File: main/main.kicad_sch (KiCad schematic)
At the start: 158 parts, among them J1 Conn_02x07_Odd_Even, J10 Conn_01x05_Pin, J2 Conn_01x02_Pin, J3 Conn_01x02_Socket, J4 Conn_01x05_Pin, J5 Conn_01x05_Pin, J6 Conn_01x05_Pin, J7 Conn_01x05_Pin, J8 Conn_01x04_Pin, J9 Conn_01x04_Pin, P1 USB_C_Plug_USB2.0, Q1 2SK2623-TL, Q10 L-31ROPT1C, Q11 L-31ROPT1C, Q12 L-31ROPT1C, Q13 L-31ROPT1C, Q14 L-31ROPT1C, Q15 L-31ROPT1C, Q16 L-31ROPT1C, Q17 L-31ROPT1C, Q18 L-31ROPT1C, Q19 L-31ROPT1C, Q2 TJ60S04M3L, Q20 2SA1015, Q21 2SA1015, Q22 2SA1015, Q23 BSS138, Q24 BSS138, Q25 2SA1015, Q3 TJ60S04M3L, Q4 L-31ROPT1C, Q5 L-31ROPT1C, Q6 L-31ROPT1C, Q7 L-31ROPT1C, Q8 L-31ROPT1C, Q9 L-31ROPT1C, SW1 SW_SPST, SW2 SW_Push, SW3 SW_Push, SW4 SW_Push, U1 OKL-T/6-W12N-C, U10 MAX3485, U2 AZ1117-3.3, U3 STM32F405RGT6, U4 BNO055, U5 MAX3485, U6 MAX3485, U7 MAX3485, U8 ESP32-WROOM-32, U9 Interface_USB_CH340K, Y1 16MHz

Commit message: メイン基板回路図完成
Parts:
- added C27, C28, C29: 0.1uF, Capacitor_SMD:C_0603_1608Metric_Pad1.08x0.95mm_HandSolder, symbol Device:C
- added D19, D20, D21: LED, LED_SMD:LED_0603_1608Metric_Pad1.05x0.95mm_HandSolder, symbol Device:LED
- added R62, R63, R64, R65, R66, R67, R68, R69, R72, R73, R74, R75, R76, R77: 10k, Resistor_SMD:R_0603_1608Metric_Pad0.98x0.95mm_HandSolder, symbol Device:R
- added R70, R71, R78: 1k, Resistor_SMD:R_0603_1608Metric_Pad0.98x0.95mm_HandSolder, symbol Device:R
- added SW10, SW5: SW_DIP_x04, Button_Switch_SMD:SW_DIP_SPSTx04_Slide_Copal_CHS-04B_W7.62mm_P1.27mm, symbol Switch:SW_DIP_x04
- added SW11, SW6, SW7: SW_SPDT, Tomoshibi_Library:SW_Slide_3P_SPDT, symbol Switch:SW_SPDT
- added SW12, SW8, SW9: SW_Push, Button_Switch_SMD:SW_Push_1P1T_NO_6x6mm_H9.5mm, symbol Switch:SW_Push
- added TP1, TP2, TP3, TP4: TestPoint, TestPoint:TestPoint_THTPad_D2.0mm_Drill1.0mm, symbol Connector:TestPoint
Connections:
- net F405RX is gone; now on net ESP_RX: U8.27 (IO16)
- net F405TX is gone; now on net ESP_TX: U8.28 (IO17)
- net +12V: now also TP1.1
- net +3.3V: now also R68.1, R69.1, R77.1, SW10.1, SW10.2, SW10.3, SW10.4, SW11.2 (B), SW5.1, SW5.2, SW5.3, SW5.4, SW6.2 (B), SW7.2 (B), TP3.1
- net +5V: now also TP2.1
- net GND: now also C27.1, C28.1, C29.1, R62.2, R63.2, R64.2, R65.2, R66.2, R67.2, R70.2, R71.2, R72.2, R73.2, R74.2, R75.2, R76.2, R78.2, SW12.2, SW8.2, SW9.2, TP4.1
- net MD_A: no longer J4.5 (Pin_5), J5.5 (Pin_5), R41.1, U5.7 (B)
- net DIPSW1: now reaches U3.2 (PC13)
- net DIPSW1: now also R63.1, SW5.7
- net DIPSW2: now reaches U3.3 (PC14)
- net DIPSW2: now also R64.1, SW5.6
- net DIPSW3: now reaches U3.4 (PC15)
- net DIPSW3: now also R65.1, SW5.5
- net LED1: now reaches U3.44 (PA11)
- net LED1: now also D20.2 (A)
- net LED0: now reaches U3.45 (PA12)
- net LED0: now also D19.2 (A)
- net TactSW1: now reaches U3.50 (PA15)
- net TactSW1: now also C28.2, R69.2, SW9.1
- net TactSW0: now reaches U3.56 (PB4)
- net TactSW0: now also C27.2, R68.2, SW8.1
- net SlideSW1: now reaches U3.57 (PB5)
- net SlideSW1: now also R67.1, SW7.1 (A)
- net SlideSW0: now reaches U3.61 (PB8)
- net SlideSW0: now also R66.1, SW6.1 (A)
- net DIPSW0: now reaches U3.62 (PB9)
- net DIPSW0: now also R62.1, SW5.8
- net ESP_SlideSW: now reaches U8.10 (IO25)
- net ESP_SlideSW: now also R76.1, SW11.1 (A)
- net ESP_TactSW: now reaches U8.11 (IO26)
- net ESP_TactSW: now also C29.2, R77.2, SW12.1
- net ESP_LED: now reaches U8.12 (IO27)
- net ESP_LED: now also D21.2 (A)
- net ESP_DIPSW0: now reaches U8.6 (IO34)
- net ESP_DIPSW0: now also R72.1, SW10.8
- net ESP_DIPSW1: now reaches U8.7 (IO35)
- net ESP_DIPSW1: now also R73.1, SW10.7
- net ESP_DIPSW2: now reaches U8.8 (IO32)
- net ESP_DIPSW2: now also R74.1, SW10.6
- net ESP_DIPSW3: now reaches U8.9 (IO33)
- net ESP_DIPSW3: now also R75.1, SW10.5
- new net: D20.1 (K), R71.1
- new net: D19.1 (K), R70.1
- new net: D21.1 (K), R78.1
- new net MD_B: J4.5 (Pin_5), J5.5 (Pin_5), R41.1, U5.7 (B)
- no-connect marks 15 -> 44
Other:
- note added: "BOOT"
- note added: "RESET"
- note added: "UI"
- note added: "サブマイコン"
- note added: "テストポイント"
- note added: "書き込み"
- moved on the sheet: C21, C22, C23, C24, P1, Q23, Q24, R53, R54, R55, R56, SW2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

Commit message: MD基板開発データ追加
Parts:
- added D22, D23, D24: LED, LED_SMD:LED_0603_1608Metric_Pad1.05x0.95mm_HandSolder, symbol Device:LED
- added R79: 6.8k, Resistor_SMD:R_0603_1608Metric_Pad0.98x0.95mm_HandSolder, symbol Device:R
- added R80: 2.2k, Resistor_SMD:R_0603_1608Metric_Pad0.98x0.95mm_HandSolder, symbol Device:R
- added R81: 1k, Resistor_SMD:R_0603_1608Metric_Pad0.98x0.95mm_HandSolder, symbol Device:R
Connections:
- net +12V: now also D22.2 (A)
- net +3.3V: now also D24.2 (A)
- net +5V: now also D23.2 (A)
- net GND: now also R79.2, R80.2, R81.2
- new net: D23.1 (K), R80.1
- new net: D24.1 (K), R81.1
- new net: D22.1 (K), R79.1
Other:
- note added: "電源LED"
- moved on the sheet: TP1, TP2, TP3, TP4

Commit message: 指摘された間違いを修正
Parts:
- removed Q1: 2SK2623-TL, Package_TO_SOT_SMD:TO-252-3_TabPin2, symbol Device:Q_NMOS_GDS
- removed R61: 10k, Resistor_SMD:R_0603_1608Metric_Pad0.98x0.95mm_HandSolder, symbol Device:R
- added F1: 20A, Tomoshibi_Library:Fuseholder_Keystone_3557, symbol Device:Fuse
- added Q1: BSS138, Package_TO_SOT_SMD:SOT-23, symbol Transistor_FET:BSS138
- R3: value 10k -> 100k
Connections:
- net +3.3V: now also Q20.1 (E), Q21.1 (E), Q22.1 (E), Q25.1 (E); no longer Q20.2 (C), Q21.2 (C), Q22.2 (C), Q25.2 (C)
- net BAT: now also F1.1; no longer Q2.2 (D), SW1.1 (A)
- net GND: now also Q1.2 (S)
- net MD_TX: no longer Q20.1 (E), R44.1, U5.2 (~{RE}), U5.3 (DE)
- net Uart1_TX: no longer Q21.1 (E), R46.1, U6.2 (~{RE}), U6.3 (DE)
- net Uart2_TX: no longer Q22.1 (E), R50.1, U7.2 (~{RE}), U7.3 (DE)
- net Uart3_TX: no longer Q25.1 (E), R58.1, U10.2 (~{RE}), U10.3 (DE)
- net at R1.1, SW1.2 (B): now also Q1.1 (G)
- net at R2.2: now also Q1.3 (D)
- new net: F1.2, Q2.2 (D), SW1.1 (A)
- new net: Q20.2 (C), R44.1, U5.2 (~{RE}), U5.3 (DE)
- new net: Q25.2 (C), R58.1, U10.2 (~{RE}), U10.3 (DE)
- new net: Q22.2 (C), R50.1, U7.2 (~{RE}), U7.3 (DE)
- new net: Q21.2 (C), R46.1, U6.2 (~{RE}), U6.3 (DE)
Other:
- moved on the sheet: C1, C2, JP1, MES1, Q2, Q3, R1, R2, R3, SW1

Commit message: 修正版回路図完成
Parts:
- removed D22: LED, LED_SMD:LED_0603_1608Metric_Pad1.05x0.95mm_HandSolder, symbol Device:LED
- removed J1: Conn_02x07_Odd_Even, Tomoshibi_Library:BoxHeader_2x07_P1.27mm_Horizontal, symbol Connector_Generic:Conn_02x07_Odd_Even
- removed J10, J7: Conn_01x05_Pin, Connector_JST:JST_XH_B5B-XH-A_1x05_P2.50mm_Vertical, symbol Connector:Conn_01x05_Pin
- removed J2: Conn_01x02_Pin, Connector_AMASS:AMASS_XT30U-M_1x02_P5.0mm_Vertical, symbol Connector:Conn_01x02_Pin
- removed J3: Conn_01x02_Socket, Connector_AMASS:AMASS_XT30U-F_1x02_P5.0mm_Vertical, symbol Connector:Conn_01x02_Socket
- removed J9: Conn_01x04_Pin, Connector_JST:JST_XH_B4B-XH-A_1x04_P2.50mm_Vertical, symbol Connector:Conn_01x04_Pin
- removed Q1, Q23, Q24: BSS138, Package_TO_SOT_SMD:SOT-23, symbol Transistor_FET:BSS138
- removed Q10, Q11, Q12, Q13, Q14, Q15, Q16, Q17, Q18, Q19, Q4, Q5, Q6, Q7, Q8, Q9: L-31ROPT1C, Tomoshibi_Library:L-31ROPT1C, symbol Device:Q_Photo_NPN
- removed Q2: TJ60S04M3L, Package_TO_SOT_THT:TO-251-3_Vertical, symbol Device:Q_PMOS_GDS
- removed Q20, Q21, Q22, Q25: 2SA1015, Package_TO_SOT_THT:TO-92_Inline, symbol Transistor_BJT:2SA1015
- removed SW4: SW_Push, Button_Switch_SMD:SW_Push_1P1T_NO_6x6mm_H9.5mm, symbol Switch:SW_Push
- removed SW5: SW_DIP_x04, Button_Switch_SMD:SW_DIP_SPSTx04_Slide_Copal_CHS-04B_W7.62mm_P1.27mm, symbol Switch:SW_DIP_x04
- removed SW7: SW_SPDT, Tomoshibi_Library:SW_Slide_3P_SPDT, symbol Switch:SW_SPDT
- removed TP2, TP3, TP4: TestPoint, TestPoint:TestPoint_THTPad_D2.0mm_Drill1.0mm, symbol Connector:TestPoint
- removed U10: MAX3485, Package_SO:SOP-8_3.76x4.96mm_P1.27mm, symbol Interface_UART:MAX3485
- removed U2: AZ1117-3.3, Package_TO_SOT_SMD:SOT-223-3_TabPin2, symbol Regulator_Linear:AZ1117-3.3
- removed U3: STM32F405RGT6, Package_QFP:LQFP-64_10x10mm_P0.5mm, symbol Tomoshibi_Library:STM32F405RGT6
- removed U4: BNO055, Tomoshibi_Library:Sensor_Motion_Aktk_BNO055, symbol Sensor_Motion:BNO055
- removed U8: ESP32-WROOM-32, RF_Module:ESP32-WROOM-32, symbol RF_Module:ESP32-WROOM-32
- removed U9: Interface_USB_CH340K, Package_SO:SSOP-10_3.9x4.9mm_P1.00mm, symbol Tomoshibi_Library:Interface_USB_CH340K
- added C30: 0.1uF, Capacitor_SMD:C_0603_1608Metric_Pad1.08x0.95mm_HandSolder, symbol Device:C
- added D22: MA10EB045, Tomoshibi_Library:Diode_DO-221BC, symbol Device:D_Schottky
- added D25: OSBL1608C1A, LED_SMD:LED_0603_1608Metric_Pad1.05x0.95mm_HandSolder, symbol Device:LED
- added J1: Conn_01x02_Pin, Connector_AMASS:AMASS_XT30U-M_1x02_P5.0mm_Vertical, symbol Connector:Conn_01x02_Pin
- added J2, J3: Conn_01x05_Pin, Connector_JST:JST_XH_B5B-XH-A_1x05_P2.50mm_Vertical, symbol Connector:Conn_01x05_Pin
- added J7: Conn_01x04_Pin, Connector_JST:JST_XH_B4B-XH-A_1x04_P2.50mm_Vertical, symbol Connector:Conn_01x04_Pin
- added J9: Conn_02x07_Odd_Even, Tomoshibi_Library:BoxHeader_2x07_P1.27mm_Horizontal, symbol Connector_Generic:Conn_02x07_Odd_Even
- added Q1: TJ60S04M3L, Tomoshibi_Library:DPAK+ 2-7M1A, symbol Device:Q_PMOS_GDS
- added Q10, Q11, Q12, Q13, Q14, Q15, Q16, Q17, Q18, Q19, Q20, Q21, Q22, Q23, Q8, Q9: NJL7502L, LED_THT:LED_D3.0mm, symbol Device:Q_Photo_NPN_EC
- added Q2: BSS138, Package_TO_SOT_SMD:SOT-23, symbol Transistor_FET:BSS138
- added Q24, Q25: 2SC3325, Package_TO_SOT_SMD:SOT-23-3, symbol Device:Q_NPN_BEC
- added Q4, Q5, Q6, Q7: 2SA1037AK, Package_TO_SOT_SMD:SOT-23-3, symbol Transistor_BJT:2SA1015
- added R61, R82: 10k, Resistor_SMD:R_0603_1608Metric_Pad0.98x0.95mm_HandSolder, symbol Device:R
- added R83: 1k, Resistor_SMD:R_0603_1608Metric_Pad0.98x0.95mm_HandSolder, symbol Device:R
- added SW4: SW_DIP_x04, Button_Switch_SMD:SW_DIP_SPSTx04_Slide_Copal_CHS-04B_W7.62mm_P1.27mm, symbol Switch:SW_DIP_x04
- added SW5: SW_SPDT, Tomoshibi_Library:SW_Slide_3P_SPDT, symbol Switch:SW_SPDT
- added SW7: SW_Push, Button_Switch_SMD:SW_Push_1P1T_NO_6x6mm_H9.5mm, symbol Switch:SW_Push
- added U10: Interface_USB_CH340K, Package_SO:SSOP-10_3.9x4.9mm_P1.00mm, symbol Tomoshibi_Library:Interface_USB_CH340K
- added U2: RT9080-33GJ5, Package_TO_SOT_SMD:TSOT-23-5, symbol Tomoshibi_Library:RT9080-33GJ5
- added U3: BNO055, Tomoshibi_Library:Sensor_Motion_Aktk_BNO055, symbol Tomoshibi_Library:BNO055
- added U4: STM32F405RGTx, Package_QFP:LQFP-64_10x10mm_P0.5mm, symbol Tomoshibi_Library:STM32F405RGTx
- added U8: MAX3485, Package_SO:SOP-8_3.76x4.96mm_P1.27mm, symbol Interface_UART:MAX3485
- added U9: ESP32-WROOM-32E, RF_Module:ESP32-WROOM-32D, symbol RF_Module:ESP32-WROOM-32E
- C13, C14: value 2.2uF -> 0.1uF
- C16, C17: value 0.1uF -> 2.2uF
- C19, C20: value 15pF -> 0.1uF
- C2: footprint Capacitor_SMD:CP_Elec_8x10 -> Capacitor_SMD:CP_Elec_8x10.5
- C23: value 0.1uF -> 22uF; footprint Capacitor_SMD:C_0603_1608Metric_Pad1.08x0.95mm_HandSolder -> Capacitor_SMD:C_0805_2012Metric_Pad1.18x1.45mm_HandSolder
- C24: value 22uF -> 0.1uF; footprint Capacitor_SMD:C_0805_2012Metric_Pad1.18x1.45mm_HandSolder -> Capacitor_SMD:C_0603_1608Metric_Pad1.08x0.95mm_HandSolder
- C5: value 10uF -> 1uF
- C6: value 22uF -> 1uF; footprint Capacitor_SMD:C_0805_2012Metric_Pad1.18x1.45mm_HandSolder -> Capacitor_SMD:C_0603_1608Metric_Pad1.08x0.95mm_HandSolder
- C7, C8: value 0.1uF -> 47pF
- D10, D11, D12, D13, D14, D15, D16, D17, D18, D6, D7, D8, D9: value OSI5120641E -> OSG8HA3Z74A; footprint LED_SMD:LED_1206_3216Metric_Pad1.42x1.75mm_HandSolder -> LED_THT:LED_D3.0mm
- D19, D20, D21: value LED -> OSG8HA3Z74A; footprint LED_SMD:LED_0603_1608Metric_Pad1.05x0.95mm_HandSolder -> LED_THT:LED_D3.0mm
- D23, D24: value LED -> OSBL1608C1A
- D3, D4, D5: value OSI5120641E -> OSR50603C1E; footprint LED_SMD:LED_1206_3216Metric_Pad1.42x1.75mm_HandSolder -> LED_SMD:LED_0603_1608Metric_Pad1.05x0.95mm_HandSolder
- Q3: footprint Package_TO_SOT_SMD:TO-252-2 -> Tomoshibi_Library:DPAK+ 2-7M1A
- R10: value 10k -> 200
- R11: value 1k -> 6.8k
- R12, R16, R20, R24, R28: value 10k -> 2.2k
- R14, R18, R22, R26: value 10k -> 7.5k
- R15, R19, R23, R27: value 1k -> 20k
- R17, R21, R25, R29: value 1k -> 2.2k
- R30, R32, R34, R36, R38, R40, R56, R72: value 10k -> 1k
- R31, R33, R35, R37, R70, R78, R8, R81, R9: value 1k -> 10k
- R4: value 1.3K -> 10k
- R41, R47, R51, R59, R80: value 2.2k -> 10k
- R42, R48, R52, R60: value 2.2k -> 1k
- R43, R45, R49, R57: value 7.5k -> 10k
- R44, R46, R50, R58: value 20k -> 1k
- R53: value 5.1k -> 10k
- R54: value 5.1k -> 1k
- R6: value 1.2k -> 1.3K
- R7: value 10k -> 1.2k
- R73, R74: value 10k -> 5.1k
- R79: value 6.8k -> 10k
- SW2: footprint Button_Switch_SMD:SW_Push_1P1T_NO_6x6mm_H9.5mm -> Tomoshibi_Library:SW_Push_6.1x6.1mm
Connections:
- net DIPSW0 is gone; now on net +3.3V: R62.1
- net LED0 is gone; now on net +3.3V: D19.2 (A)
- net LED1 is gone; now on net +3.3V: D20.2 (A)
- net MD_TX is gone; now on net MAIN_RX/MD_TX: U5.1 (RO)
- net Uart1_TX is gone; now on net MAIN1_RX/Device1_TX: U6.1 (RO)
- net Uart2_TX is gone; now on net MAIN2_RX/Device2_TX: U7.1 (RO)
- net Uart3_A is gone; now on net GND: R59.2
- net Uart3_B is gone; now on an unnamed net: R60.1
- net Uart3_RX is gone; now on net Line13: R57.1
- net +12V: now also D3.2 (A), D22.2 (A); no longer J4.2 (Pin_2), J5.2 (Pin_2), J6.2 (Pin_2), TP1.1
- net +3.3V: now also C13.1, C14.1, C15.1, C19.1, C20.1, C22.1, C23.1, C29.1, D21.2 (A), R16.1, R20.1, R24.1, R28.1, R70.1, R8.1, R9.1, J9.3 (Pin_3), Q10.2 (C), Q11.2 (C), Q12.2 (C), Q13.2 (C), Q14.2 (C), Q15.2 (C), Q16.2 (C), Q17.2 (C), Q18.2 (C), Q19.2 (C), Q20.2 (C), Q21.2 (C), Q22.2 (C), Q23.2 (C), Q4.1 (E), Q5.1 (E), Q6.1 (E), Q7.1 (E), Q8.2 (C), Q9.2 (C), R82.1, SW4.1, SW4.2, SW4.3, SW4.4, SW5.2 (B), U10.10 (V3), U10.7 (VCC), U3.1 (VIN), U4.1 (VBAT), U4.13 (VDDA), U4.19 (VDD), U4.32 (VDD), U4.48 (VDD), U4.64 (VDD), U8.8 (VCC), U9.2 (VDD); no longer C15.2, C16.1, C17.1, C24.1, C25.1, C6.1, C7.1, C8.1, C9.1, D2.2 (A), D24.2 (A), D3.2 (A), D4.2 (A), R39.1, R40.1, R42.1, R47.1, R51.1, R55.1, R56.1, R59.1, R68.1, R77.1
- net +5V: now also D4.2 (A), R7.1, J2.3 (Pin_3), J3.3 (Pin_3), J7.2 (Pin_2), U2.1 (VIN), U2.3 (EN); no longer D23.2 (A), R6.1
- net BAT: now also J1.2 (Pin_2)
- net BOOT: now also C28.2, SW9.1, Q25.3 (C), U9.25 (IO0); no longer C23.2, R56.2, SW3.1
- net ESP_DIPSW0: now also R77.1, U9.6 (IO34); no longer R72.1
- net ESP_DIPSW1: now also R78.1, U9.7 (IO35); no longer R73.1
- net ESP_DIPSW2: now also R79.1, U9.8 (IO32); no longer R74.1
- net ESP_DIPSW3: now also R80.1, U9.9 (IO33); no longer R75.1
- net ESP_LED: now also D25.2 (A), U9.12 (IO27); no longer D21.2 (A)
- net ESP_SlideSW: now also R81.1, U9.10 (IO25); no longer R76.1
- net ESP_TactSW: now also C30.2, R82.2, U9.11 (IO26); no longer C29.2, R77.2
- net GND: now also C15.2, C22.2, C23.2, C24.1, C25.1, C27.2, C29.2, C9.1, R2.2, R39.2, R40.2, R42.2, R43.2, R45.2, R47.2, R49.2, R51.2, R55.2, R56.2, R57.2, R68.2, R77.2, TP1.1, C30.1, J1.1 (Pin_1), J2.1 (Pin_1), J3.1 (Pin_1), J7.1 (Pin_1), J9.11 (Pin_11), J9.5 (Pin_5), J9.7 (Pin_7), Q1.1 (G), Q2.2 (S), R61.2, R83.2, SW7.2, U10.3 (GND), U2.2 (GND), U2.4 (NC), U3.2 (GND), U3.7 (GND), U4.12 (VSSA), U4.18 (VSS), U4.60 (BOOT0), U4.63 (VSS), U8.5 (GND), U9.1 (GND), U9.15 (GND), U9.38 (GND), U9.39 (GND); no longer C15.1, C22.1, C23.1, C24.2, C25.2, C27.1, C29.1, C9.2, R10.2, R14.2, R16.2, R18.2, R20.2, R22.2, R24.2, R26.2, R28.2, R4.2, R62.2, R70.2, R75.2, R76.2, R8.2, R9.2
- net Gyro_SCL: now also R9.2, U3.4 (SCL/R), U4.58 (PB6); no longer R40.2
- net Gyro_SDA: now also R8.2, U3.3 (SDA/T), U4.59 (PB7); no longer R39.2
- net Line0: now also R31.1, Q8.1 (E), U4.8 (PC0); no longer R7.1
- net Line1: now also R33.1, Q9.1 (E), U4.9 (PC1); no longer R10.1
- net Line10: now also R51.1, Q18.1 (E), U4.22 (PA6); no longer R28.1
- net Line11: now also R53.1, Q19.1 (E), U4.23 (PA7); no longer R30.1
- net Line12: now also R55.1, Q20.1 (E), U4.24 (PC4); no longer R32.1
- net Line13: now also Q21.1 (E), U4.25 (PC5); no longer R34.1
- net Line14: now also R59.1, Q22.1 (E), U4.26 (PB0); no longer R36.1
- net Line15: now also Q23.1 (E), R61.1, U4.27 (PB1); no longer R38.1
- net Line2: now also R35.1, Q10.1 (E), U4.10 (PC2); no longer R12.1
- net Line3: now also R37.1, Q11.1 (E), U4.11 (PC3); no longer R14.1
- net Line4: now also R39.1, Q12.1 (E), U4.14 (PA0); no longer R16.1
- net Line5: now also R41.1, Q13.1 (E), U4.15 (PA1); no longer R18.1
- net Line6: now also R43.1, Q14.1 (E), U4.16 (PA2); no longer R20.1
- net Line7: now also R45.1, Q15.1 (E), U4.17 (PA3); no longer R22.1
- net Line8: now also R47.1, Q16.1 (E), U4.20 (PA4); no longer R24.1
- net Line9: now also R49.1, Q17.1 (E), U4.21 (PA5); no longer R26.1
- net MD_A: now also R16.2, J2.4 (Pin_4), J3.4 (Pin_4); no longer J4.4 (Pin_4), J5.4 (Pin_4), R42.2
- net MD_B: now also R17.1, J2.5 (Pin_5), J3.5 (Pin_5); no longer J4.5 (Pin_5), J5.5 (Pin_5), R41.1
- net NRST: now also C9.2, SW2.1, J9.12 (Pin_12), U4.7 (NRST); no longer C26.2
- net RCC_OSC_IN: now also C7.1, U4.5 (PH0); no longer C19.1
- net RCC_OSC_OUT: now also R10.2, U4.6 (PH1); no longer C20.1, Y1.1
- net RESET: now also C24.2, C27.1, R62.2, SW3.1, Q24.3 (C), U9.3 (EN); no longer C22.2, R55.2, SW2.1
- net SWCLk: now also J9.6 (Pin_6), U4.49 (PA14)
- net SWDIO: now also J9.4 (Pin_4), U4.46 (PA13)
- net SWO: now also J9.8 (Pin_8), U4.55 (PB3)
- net TIM1_CH1: now also J7.3 (Pin_3), U4.41 (PA8); no longer J8.3 (Pin_3)
- net TIM1_CH1N: now also J7.4 (Pin_4), U4.34 (PB13); no longer J8.4 (Pin_4)
- net TIM8_CH3: now also J8.3 (Pin_3), U4.39 (PC8)
- net TIM8_CH3N: now also J8.4 (Pin_4), U4.36 (PB15)
- net VCAP1: now also C16.1, U4.31 (VCAP_1); no longer C13.1
- net VCAP2: now also C17.1, U4.47 (VCAP_2); no longer C14.1
- net at SW1.1 (B): now also R2.1, Q2.1 (G); no longer F1.2
- net at R1.1, SW1.2 (A): now also C1.1, Q3.3 (S), R3.1, Q1.3 (S)
- net at R11.1: now also D3.1 (K); no longer D5.1 (K)
- net at D18.1 (K): now also R54.1; no longer R37.1
- net MAIN_RX/MD_TX: now reaches U5.2 (~{RE}), U5.3 (DE)
- net MAIN_RX/MD_TX: now also R15.1, Q4.2 (C), U4.43 (PA10); no longer R44.1
- net at D23.1 (K): now also R71.1; no longer R80.1
- net at D4.1 (K): now also R12.1; no longer R9.1
- net at P1.B5 (CC2): now also R73.1; no longer R53.1
- net at D20.1 (K): now also R58.1; no longer R71.1
- net at D17.1 (K): now also R52.1; no longer R35.1
- net at D11.1 (K): now also R40.1; no longer R23.1
- net at C1.2, Q3.1 (G), R3.2: now also R4.1; no longer R2.1
- net at D8.1 (K): now also R34.1; no longer R17.1
- net at U1.6 (TRIM): now also R6.1; no longer R4.1
- net at P1.A5 (CC1): now also R74.1; no longer R54.1
- net at P1.A6 (D+): now also U10.1 (UD+)
- net at P1.A7 (D-): now also U10.2 (UD-)
- net at D16.1 (K): now also R50.1; no longer R33.1
- net at D14.1 (K): now also R46.1; no longer R29.1
- net at D19.1 (K): now also R56.1; no longer R70.1
- net at D15.1 (K): now also R48.1; no longer R31.1
- net at D24.1 (K): now also R72.1; no longer R81.1
- net at D9.1 (K): now also R36.1; no longer R19.1
- net at D21.1 (K): no longer R78.1
- net at D6.1 (K): now also R30.1; no longer R13.1
- net MAIN2_RX/Device2_TX: now reaches U7.2 (~{RE}), U7.3 (DE)
- net MAIN2_RX/Device2_TX: now also R23.1, Q6.2 (C), U4.54 (PD2); no longer R50.1
- net MAIN1_RX/Device1_TX: now reaches U6.2 (~{RE}), U6.3 (DE)
- net MAIN1_RX/Device1_TX: now also R19.1, Q5.2 (C), U4.52 (PC11); no longer R46.1
- net at D10.1 (K): now also R38.1; no longer R21.1
- net at D7.1 (K): now also R32.1; no longer R15.1
- net at D12.1 (K): now also R42.1; no longer R25.1
- net at D13.1 (K): now also R44.1; no longer R27.1
- net DIPSW1 renamed F405_DIPSW0
- net F405_DIPSW0: now also SW4.8, U4.62 (PB9)
- net DIPSW2 renamed F405_DIPSW1
- net F405_DIPSW1: now also SW4.7, U4.2 (PC13)
- net DIPSW3 renamed F405_DIPSW2
- net F405_DIPSW2: now also SW4.6, U4.3 (PC14)
- net MD_RX renamed MAIN_TX/MD_RX
- net MAIN_TX/MD_RX: now also R14.1, U4.42 (PA9); no longer R43.1
- net SlideSW0 renamed F405_DIPSW3
- net F405_DIPSW3: now also SW4.5, U4.4 (PC15); no longer SW6.1 (A)
- net SlideSW1 renamed F405_SlideSW0
- net F405_SlideSW0: now also SW5.1 (A), U4.61 (PB8)
- removed net TactSW0: C27.2, R68.2, SW8.1
- removed net TactSW1: C28.2, R69.2, SW9.1
- removed net Uart1_A: J6.4 (Pin_4), R47.2, U6.6 (A)
- removed net Uart1_B: J6.5 (Pin_5), R48.1, U6.7 (B)
- net Uart1_RX renamed MAIN1_TX/Device1_RX
- net MAIN1_TX/Device1_RX: now also R18.1, U4.51 (PC10); no longer R45.1
- net Uart2_A renamed Device2_A
- net Device2_A: now also J5.4 (Pin_4), R24.2; no longer R51.2
- net Uart2_B renamed Device2_B
- net Device2_B: now also J5.5 (Pin_5), R25.1; no longer R52.1
- net Uart2_RX renamed MAIN2_TX/Device2_RX
- net MAIN2_TX/Device2_RX: now also R22.1, U4.53 (PC12); no longer R49.1
- new net: Q2.3 (D), R4.2
- new net: Q6.3 (B), R22.2
- new net: Q25.2 (E), R75.1, U10.4 (~{DTR})
- new net: Q24.2 (E), R76.1, U10.6 (~{RTS})
- new net: Q24.1 (B), R75.2
- new net: C8.1, R10.1, Y1.1
- new net: Q4.3 (B), R14.2
- new net: F1.2, Q1.2 (D)
- new net: Q25.1 (B), R76.2
- new net: D25.1 (K), R83.1
- new net: D5.1 (K), R13.1
- new net: Q7.3 (B), R26.2
- new net: Q5.3 (B), R18.2
- new net +3V3: C6.1, D2.2 (A), U2.5 (VOUT)
- new net Device1_A: J4.4 (Pin_4), R20.2, U6.6 (A)
- new net Device1_B: J4.5 (Pin_5), R21.1, U6.7 (B)
- new net Device3_A: J6.4 (Pin_4), R28.2, U8.6 (A)
- new net Device3_B: J6.5 (Pin_5), R29.1, U8.7 (B)
- new net ESP_RX/CH340_TX: U10.8 (TXD), U9.34 (RXD0/IO3)
- new net ESP_TX/CH340_RX: U10.9 (RXD), U9.35 (TXD0/IO1)
- new net F405_LED0: D23.2 (A), U4.45 (PA12)
- new net F405_LED1: D24.2 (A), U4.44 (PA11)
- new net F405_SlideSW1: R68.1, SW6.1 (A), U4.57 (PB5)
- new net F405_TactSW0: C25.2, R69.2, SW7.1, U4.56 (PB4)
- new net F405_TactSW1: C26.2, R70.2, SW8.1, U4.50 (PA15)
- new net MAIN3_RX/Device3_TX: Q7.2 (C), R27.1, U4.30 (PB11), U8.1 (RO), U8.2 (~{RE}), U8.3 (DE)
- new net MAIN3_TX/Device3_RX: R26.1, U4.29 (PB10), U8.4 (DI)
- new net MAIN_RX/ESP_TX: U4.38 (PC7), U9.28 (IO17)
- new net MAIN_TX/ESP_RX: U4.37 (PC6), U9.27 (IO16)
- new net PWR: D22.1 (K), J2.2 (Pin_2), J3.2 (Pin_2), J4.2 (Pin_2), J5.2 (Pin_2), J6.2 (Pin_2)
- no-connect marks 44 -> 36
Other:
- note added: "BOOT・RESET"
- note added: "ESP32"
- note added: "ESP書き込み"
- note added: "F405"
- note added: "RS485"
- note added: "コネクタ"
- note added: "ラインセンサ"
- note added: "保護回路・スイッチ"
- note added: "水晶"
- note added: "電源LED・テストポイント"
- note removed: "BOOT"
- note removed: "RESET"
- note removed: "RS485変換"
- note removed: "コネクター"
- note removed: "サブマイコン"
- note removed: "テストポイント"
- note removed: "メインマイコン"
- note removed: "ラインセンサー"
- note removed: "書き込み"
- note removed: "水晶振動子"
- note removed: "電源LED"
- note removed: "電源スイッチ・保護回路"

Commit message: 回路図完成
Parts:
- D1, D2: value SBR1A40SA -> CUS01; footprint Diode_SMD:D_SMA_Handsoldering -> Diode_SMD:D_SOD-323_HandSoldering
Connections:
- net SWCLk renamed SWCLK
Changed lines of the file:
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@@
     )
   )
-  (global_label "SWCLk" (shape bidirectional) (at 260.35 109.22 90) (fields_autoplaced)
+  (global_label "SWCLK" (shape bidirectional) (at 260.35 109.22 90) (fields_autoplaced)
     (effects (font (size 1.27 1.27)) (justify left))
-    (property "Intersheetrefs" "${INTERSHEET_REFS}" (at 260.35 99.1364 90)
+    (property "Intersheetrefs" "${INTERSHEET_REFS}" (at 260.35 98.8945 90)
       (effects (font (size 1.27 1.27)) (justify left) hide)
     )
@@
     )
   )
-  (global_label "SWCLk" (shape bidirectional) (at 40.64 127 0) (fields_autoplaced)
+  (global_label "SWCLK" (shape bidirectional) (at 40.64 127 0) (fields_autoplaced)
     (effects (font (size 1.27 1.27)) (justify left))
-    (property "Intersheetrefs" "${INTERSHEET_REFS}" (at 50.7236 127 0)
+    (property "Intersheetrefs" "${INTERSHEET_REFS}" (at 50.9655 127 0)
       (effects (font (size 1.27 1.27)) (justify left) hide)
     )
@@
     )
   )
-  (symbol (lib_id "Device:D_Schottky") (at 215.9 25.4 0) (unit 1)
-    (in_bom yes) (on_board yes) (dnp no) (fields_autoplaced)
-    (property "Reference" "D2" (at 215.5825 19.05 0)
-      (effects (font (size 1.27 1.27)))
-    )
-    (property "Value" "SBR1A40SA" (at 215.5825 21.59 0)
-      (effects (font (size 1.27 1.27)))
-    )
-    (property "Footprint" "Diode_SMD:D_SMA_Handsoldering" (at 215.9 25.4 0)
-      (effects (font (size 1.27 1.27)) hide)
-    )
-    (property "Datasheet" "~" (at 215.9 25.4 0)
-      (effects (font (size 1.27 1.27)) hide)
-    )
-    (pin "2")
-    (pin "1")
-    (instances
-      (project "MAIN"
-        (path "/ecf1504d-7b9a-404b-bd65-805b54c9eb1d"
-          (reference "D2") (unit 1)
-        )
-      )
-    )
-  )
   (symbol (lib_id "Device:Q_Photo_NPN_EC") (at 187.96 210.82 0) (unit 1)
     (in_bom yes) (on_board yes) (dnp no) (fields_autoplaced)
@@
     )
   )
+  (symbol (lib_id "Device:D_Schottky") (at 215.9 25.4 0) (unit 1)
+    (in_bom yes) (on_board yes) (dnp no) (fields_autoplaced)
+    (property "Reference" "D2" (at 215.5825 19.05 0)
+      (effects (font (size 1.27 1.27)))
+    )
+    (property "Value" "CUS01" (at 215.5825 21.59 0)
+      (effects (font (size 1.27 1.27)))
+    )
+    (property "Footprint" "Diode_SMD:D_SOD-323_HandSoldering" (at 215.9 25.4 0)
+      (effects (font (size 1.27 1.27)) hide)
+    )
+    (property "Datasheet" "~" (at 215.9 25.4 0)
+      (effects (font (size 1.27 1.27)) hide)
+    )
+    (pin "2")
+    (pin "1")
+    (instances
+      (project "MAIN"
+        (path "/ecf1504d-7b9a-404b-bd65-805b54c9eb1d"
+          (reference "D2") (unit 1)
+        )
+      )
+    )
+  )
   (symbol (lib_id "Transistor_BJT:2SA1015") (at 171.45 359.41 0) (mirror x) (unit 1)
     (in_bom yes) (on_board yes) (dnp no)
@@
       (effects (font (size 1.27 1.27)))
     )
-    (property "Value" "SBR1A40SA" (at 148.2725 21.59 0)
+    (property "Value" "CUS01" (at 148.2725 21.59 0)
       (effects (font (size 1.27 1.27)))
     )
-    (property "Footprint" "Diode_SMD:D_SMA_Handsoldering" (at 148.59 25.4 0)
+    (property "Footprint" "Diode_SMD:D_SOD-323_HandSoldering" (at 148.59 25.4 0)
       (effects (font (size 1.27 1.27)) hide)
     )

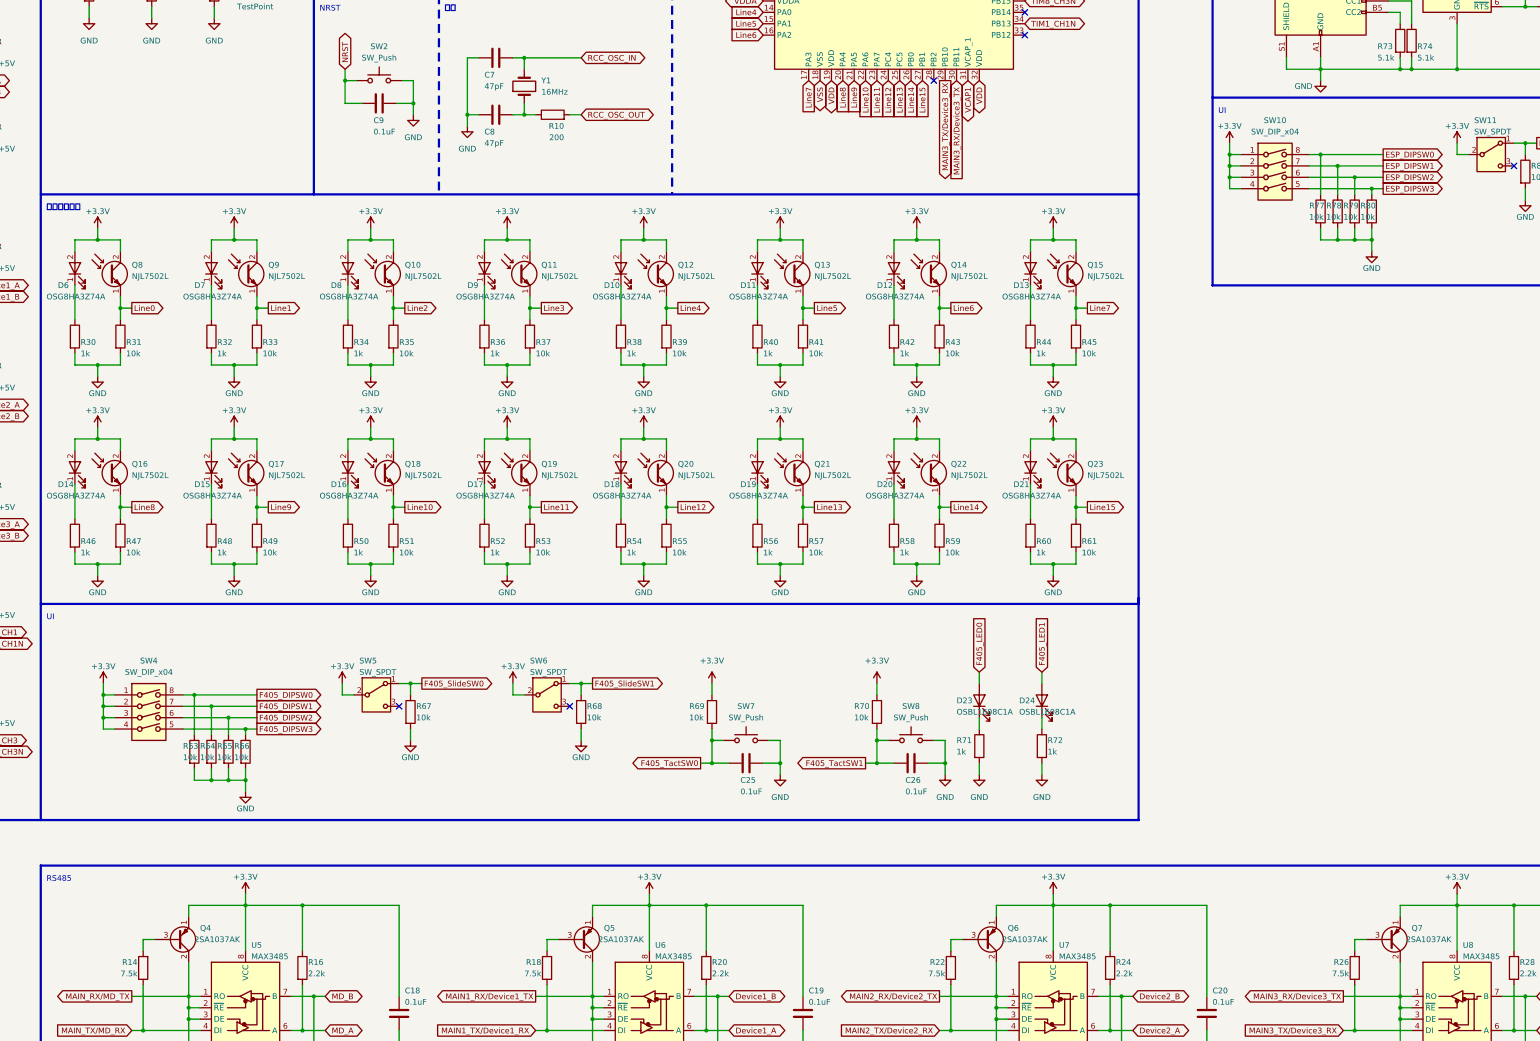
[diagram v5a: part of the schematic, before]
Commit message: MDの回路を変更
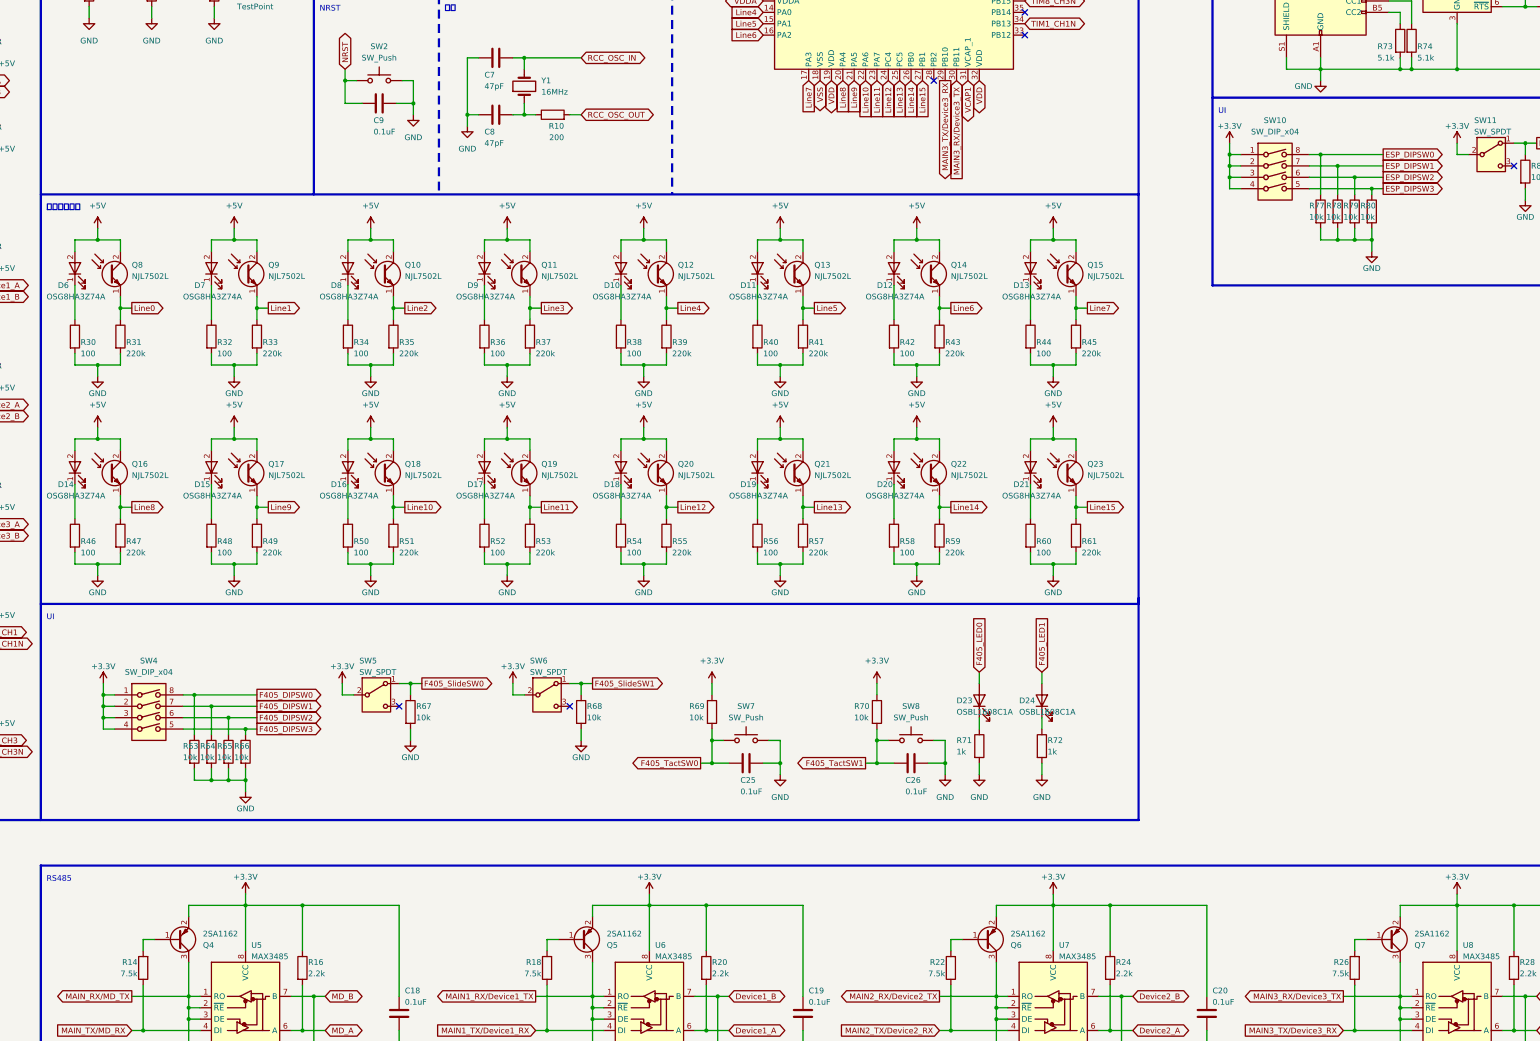
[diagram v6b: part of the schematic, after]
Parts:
- removed Q4, Q5, Q6, Q7: 2SA1037AK, Package_TO_SOT_SMD:SOT-23-3, symbol Transistor_BJT:2SA1015
- added Q4, Q5, Q6, Q7: 2SA1162, Package_TO_SOT_SMD:SOT-23-3, symbol Device:Q_PNP_BEC
- J1: footprint Connector_AMASS:AMASS_XT30U-M_1x02_P5.0mm_Vertical -> Connector_AMASS:AMASS_XT60-M_1x02_P7.20mm_Vertical
- R30, R32, R34, R36, R38, R40, R42, R44, R46, R48, R50, R52, R54, R56, R58, R60: value 1k -> 100
- R31, R33, R35, R37, R39, R41, R43, R45, R47, R49, R51, R53, R55, R57, R59, R61: value 10k -> 220k
- SW2: footprint Tomoshibi_Library:SW_Push_6.1x6.1mm -> Button_Switch_SMD:SW_Push_1P1T_NO_6x6mm_H9.5mm
- U3: footprint Tomoshibi_Library:Sensor_Motion_Aktk_BNO055 -> MyLibrary:BNO055
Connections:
- net +3.3V: now also Q4.2 (E), Q5.2 (E), Q6.2 (E), Q7.2 (E); no longer D10.2 (A), D11.2 (A), D12.2 (A), D13.2 (A), D14.2 (A), D15.2 (A), D16.2 (A), D17.2 (A), D18.2 (A), D19.2 (A), D20.2 (A), D21.2 (A), D6.2 (A), D7.2 (A), D8.2 (A), D9.2 (A), Q10.2 (C), Q11.2 (C), Q12.2 (C), Q13.2 (C), Q14.2 (C), Q15.2 (C), Q16.2 (C), Q17.2 (C), Q18.2 (C), Q19.2 (C), Q20.2 (C), Q21.2 (C), Q22.2 (C), Q23.2 (C), Q8.2 (C), Q9.2 (C)
- net +5V: now also D10.2 (A), D11.2 (A), D12.2 (A), D13.2 (A), D14.2 (A), D15.2 (A), D16.2 (A), D17.2 (A), D18.2 (A), D19.2 (A), D20.2 (A), D21.2 (A), D6.2 (A), D7.2 (A), D8.2 (A), D9.2 (A), Q10.2 (C), Q11.2 (C), Q12.2 (C), Q13.2 (C), Q14.2 (C), Q15.2 (C), Q16.2 (C), Q17.2 (C), Q18.2 (C), Q19.2 (C), Q20.2 (C), Q21.2 (C), Q22.2 (C), Q23.2 (C), Q8.2 (C), Q9.2 (C)
- net MAIN1_RX/Device1_TX: now also Q5.3 (C)
- net MAIN2_RX/Device2_TX: now also Q6.3 (C)
- net MAIN3_RX/Device3_TX: now also Q7.3 (C)
- net MAIN_RX/MD_TX: now also Q4.3 (C)
- net at R22.2: now also Q6.1 (B)
- net at R14.2: now also Q4.1 (B)
- net at R26.2: now also Q7.1 (B)
- net at R18.2: now also Q5.1 (B)
